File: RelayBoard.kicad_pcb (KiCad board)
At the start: 4 copper layers, 254 x 105.6 mm, 151 parts, among them J1 CONN_03-SCREW-5MM, J11 CONN_03-SCREW-5MM, J12 CONN_03-SCREW-5MM, J13 CONN_03-SCREW-5MM, J14 CONN_03-SCREW-5MM, J15 CONN_03-SCREW-5MM, J16 CONN_03-SCREW-5MM, J17 CONN_03-SCREW-5MM, J18 CONN_03-SCREW-5MM, J2 CONN_03-SCREW-5MM, J22 Conn_01x04, J24 Conn_01x06, J3 CONN_03-SCREW-5MM, J4 CONN_03-SCREW-5MM, J5 CONN_03-SCREW-5MM, J6 CONN_03-SCREW-5MM, J7 CONN_03-SCREW-5MM, J8 CONN_03-SCREW-5MM, K1 SANYOU_SRD_Form_C, K11 SANYOU_SRD_Form_C, K12 SANYOU_SRD_Form_C, K13 SANYOU_SRD_Form_C, K14 SANYOU_SRD_Form_C, K15 SANYOU_SRD_Form_C, K16 SANYOU_SRD_Form_C, K17 SANYOU_SRD_Form_C, K18 SANYOU_SRD_Form_C, K2 SANYOU_SRD_Form_C, K3 SANYOU_SRD_Form_C, K4 SANYOU_SRD_Form_C, K5 SANYOU_SRD_Form_C, K6 SANYOU_SRD_Form_C, K7 SANYOU_SRD_Form_C, K8 SANYOU_SRD_Form_C, Q1 ULN2803ADWR, Q2 ULN2803ADWR, U1 AP1117-33, U2 NodeMCUDevKitV1, U3 LTV-847, U4 LTV-847, U5 LTV-847, U6 LTV-847

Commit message: basic design with solid state relays complete
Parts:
- removed D11, D111, D112, D113, D114, D115, D116, D117, D118, D12, D13, D14, D15, D16, D17, D18: 1N4148W, Diode_SMD:D_SOD-123
- removed K1, K11, K12, K13, K14, K15, K16, K17, K18, K2, K3, K4, K5, K6, K7, K8: SANYOU_SRD_Form_C, Relay_THT:Relay_SPDT_SANYOU_SRD_Series_Form_C
- removed R1, R2: 22, Resistor_SMD:R_0402_1005Metric
- removed R12, R13, R14, R15, R16, R17, R18, R19, R20, R21, R22, R23, R24, R25, R26, R27: 150, Resistor_SMD:R_0402_1005Metric
- removed R3: 1.3k, Resistor_SMD:R_0402_1005Metric
- added U1: TLP148G, Package_SO:MFSOP6-5_4.4x3.6mm_P1.27mm, F.Cu at (140.0, 80.9)
- added U11: TLP148G, Package_SO:MFSOP6-5_4.4x3.6mm_P1.27mm, F.Cu at (157.5, 81.8)
- added U12: TLP148G, Package_SO:MFSOP6-5_4.4x3.6mm_P1.27mm, F.Cu at (174.9, 81.9)
- added U13: TLP148G, Package_SO:MFSOP6-5_4.4x3.6mm_P1.27mm, F.Cu at (192.1, 82.2)
- added U14: TLP148G, Package_SO:MFSOP6-5_4.4x3.6mm_P1.27mm, F.Cu at (209.8, 82.2)
- added U15: TLP148G, Package_SO:MFSOP6-5_4.4x3.6mm_P1.27mm, F.Cu at (210.0, 145.5)
- added U16: TLP148G, Package_SO:MFSOP6-5_4.4x3.6mm_P1.27mm, F.Cu at (192.5, 145.3)
- added U17: TLP148G, Package_SO:MFSOP6-5_4.4x3.6mm_P1.27mm, F.Cu at (175.2, 145.3)
- added U18: TLP148G, Package_SO:MFSOP6-5_4.4x3.6mm_P1.27mm, F.Cu at (157.5, 145.4)
- added U2: TLP148G, Package_SO:MFSOP6-5_4.4x3.6mm_P1.27mm, F.Cu at (122.4, 81.0)
- added U7: TLP148G, Package_SO:MFSOP6-5_4.4x3.6mm_P1.27mm, F.Cu at (105.0, 145.9)
- added U8: TLP148G, Package_SO:MFSOP6-5_4.4x3.6mm_P1.27mm, F.Cu at (87.5, 146.1)
- U3, U4, U5, U6: value LTV-847 -> TLP148G; footprint digikey-footprints:DIP-16_W7.62mm -> Package_SO:MFSOP6-5_4.4x3.6mm_P1.27mm
- moved J8 180.4 mm to (92.5, 155.4), turned to 180 degrees
- moved D38 178.8 mm to (87.5, 140.9), turned to -90 degrees
- moved R208 176.6 mm to (86.0, 140.9), turned to 90 degrees
- moved R108 164.9 mm to (89.1, 140.9), turned to 90 degrees
- moved J7 149.4 mm to (110.0, 155.3), turned to 180 degrees
- moved D37 142.0 mm to (105.0, 140.8), turned to -90 degrees
- moved R207 141.2 mm to (103.4, 140.8), turned to 90 degrees
- moved Q1 137.4 mm to (84.6, 117.4), turned to 180 degrees
- moved R4 129.5 mm to (28.2, 154.0), turned to 90 degrees
- moved R107 129.0 mm to (106.6, 140.8), turned to 90 degrees
- moved J14 124.0 mm to (204.8, 72.6), turned to 0 degrees
- moved J6 122.4 mm to (127.4, 155.0), turned to 180 degrees
- moved R214 116.7 mm to (211.3, 87.3), turned to -90 degrees
- moved D314 116.1 mm to (209.8, 87.3), turned to 90 degrees
- moved D36 108.6 mm to (122.4, 140.6), turned to -90 degrees
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- renumbered U2 to UM2, U1 to UP1
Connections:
- Q1 pad 11: Net-(Q1-Pad11) -> Net-(R108-Pad1)
- Q1 pad 12: Net-(Q1-Pad12) -> Net-(R107-Pad1)
- Q1 pad 13: Net-(Q1-Pad13) -> Net-(R106-Pad1)
- Q1 pad 14: Net-(Q1-Pad14) -> Net-(R105-Pad1)
- Q1 pad 15: Net-(Q1-Pad15) -> Net-(R103-Pad1)
- Q1 pad 16: Net-(Q1-Pad16) -> Net-(R104-Pad1)
- Q1 pad 17: Net-(Q1-Pad17) -> Net-(R102-Pad1)
- Q1 pad 18: Net-(Q1-Pad18) -> Net-(R101-Pad1)
- Q2 pad 11: Net-(Q2-Pad11) -> Net-(R118-Pad1)
- Q2 pad 13: Net-(Q2-Pad13) -> Net-(R116-Pad1)
- Q2 pad 14: Net-(Q2-Pad14) -> Net-(R115-Pad1)
- Q2 pad 15: Net-(Q2-Pad15) -> Net-(R114-Pad1)
- Q2 pad 16: Net-(Q2-Pad16) -> Net-(R113-Pad1)
- Q2 pad 17: Net-(Q2-Pad17) -> Net-(R112-Pad1)
- Q2 pad 18: Net-(Q2-Pad18) -> Net-(R111-Pad1)
- R101 pad 1: Net-(D11-Pad1) -> Net-(R101-Pad1)
- R102 pad 1: Net-(D12-Pad1) -> Net-(R102-Pad1)
- R103 pad 1: Net-(D13-Pad1) -> Net-(R103-Pad1)
- R104 pad 1: Net-(D14-Pad1) -> Net-(R104-Pad1)
- R105 pad 1: Net-(D15-Pad1) -> Net-(R105-Pad1)
- R106 pad 1: Net-(D16-Pad1) -> Net-(R106-Pad1)
- R107 pad 1: Net-(D17-Pad1) -> Net-(R107-Pad1)
- R108 pad 1: Net-(D18-Pad1) -> Net-(R108-Pad1)
- R111 pad 1: Net-(D111-Pad1) -> Net-(R111-Pad1)
- R112 pad 1: Net-(D112-Pad1) -> Net-(R112-Pad1)
- R113 pad 1: Net-(D113-Pad1) -> Net-(R113-Pad1)
- R114 pad 1: Net-(D114-Pad1) -> Net-(R114-Pad1)
- R115 pad 1: Net-(D115-Pad1) -> Net-(R115-Pad1)
- R116 pad 1: Net-(D116-Pad1) -> Net-(R116-Pad1)
- R117 pad 1: Net-(D117-Pad1) -> Net-(Q2-Pad12)
- R118 pad 1: Net-(D118-Pad1) -> Net-(R118-Pad1)
- U3 pad 1: Net-(Q1-Pad18) -> Net-(R103-Pad1)
- U3 pad 3: Net-(Q1-Pad17) -> Net-(D33-Pad2)
- U3 pad 4: Net-(R20-Pad2) -> Net-(J3-Pad3)
- U3 pad 5: Net-(Q1-Pad16) -> Net-(J3-Pad2)
- U3 pad 6: Net-(R21-Pad2) -> Net-(J3-Pad1)
- U4 pad 1: Net-(Q2-Pad18) -> Net-(R104-Pad1)
- U4 pad 3: Net-(Q2-Pad17) -> Net-(D34-Pad2)
- U4 pad 4: Net-(R13-Pad2) -> Net-(J4-Pad3)
- U4 pad 5: Net-(Q2-Pad16) -> Net-(J4-Pad2)
- U4 pad 6: Net-(R14-Pad2) -> Net-(J4-Pad1)
- U5 pad 1: Net-(Q1-Pad14) -> Net-(R105-Pad1)
- U5 pad 3: Net-(Q1-Pad13) -> Net-(D35-Pad2)
- U5 pad 4: Net-(R24-Pad2) -> Net-(J5-Pad3)
- U5 pad 5: Net-(Q1-Pad12) -> Net-(J5-Pad2)
- U5 pad 6: Net-(R25-Pad2) -> Net-(J5-Pad1)
- U6 pad 1: Net-(Q2-Pad14) -> Net-(R106-Pad1)
- U6 pad 3: Net-(Q2-Pad13) -> Net-(D36-Pad2)
- U6 pad 4: Net-(R17-Pad2) -> Net-(J6-Pad3)
- U6 pad 5: Net-(Q2-Pad12) -> Net-(J6-Pad2)
- U6 pad 6: Net-(R18-Pad2) -> Net-(J6-Pad1)
- UM2 pad 10: unconnected-(U2-Pad10) -> LED3
- UM2 pad 11: unconnected-(U2-Pad11) -> LED4
- UM2 pad 3: (no net) -> VBUS
- UM2 pad 4: (no net) -> MCU_VCC
- UM2 pad 5: unconnected-(U2-Pad5) -> LED1
- UM2 pad 6: (no net) -> GND
- UM2 pad 8: unconnected-(U2-Pad8) -> LED2
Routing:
- net Net-(Q1-Pad1): track 0.00 -> 107.7 mm
- net Net-(Q1-Pad2): track 0.00 -> 102.7 mm
- net Net-(Q2-Pad1): track 0.00 -> 97.9 mm, vias 0 -> 1
- net Net-(Q1-Pad3): track 0.00 -> 97.8 mm
- net Net-(Q2-Pad2): track 0.00 -> 96.7 mm, vias 0 -> 1
- net Net-(Q2-Pad3): track 0.00 -> 95.6 mm, vias 0 -> 1
- net Net-(Q2-Pad4): track 0.00 -> 94.3 mm, vias 0 -> 1
- net Net-(Q2-Pad5): track 0.00 -> 93.2 mm, vias 0 -> 1
- net Net-(Q1-Pad4): track 0.00 -> 92.7 mm
- net Net-(Q2-Pad6): track 0.00 -> 91.9 mm, vias 0 -> 1
- net Net-(Q2-Pad7): track 0.00 -> 90.8 mm, vias 0 -> 1
- net Net-(Q2-Pad8): track 0.00 -> 90.7 mm, vias 0 -> 1
- net Net-(Q1-Pad5): track 0.00 -> 87.8 mm
- net Net-(Q1-Pad6): track 0.00 -> 82.8 mm
- net Net-(R115-Pad1): track 0.00 -> 79.7 mm
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- added copper zone on F.Cu, net GND
- added copper zone on In1.Cu, net GND
- added copper zone on B.Cu, net MCU_VCC
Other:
- board size 254 x 105.6 mm -> 210.4 x 94.7 mm

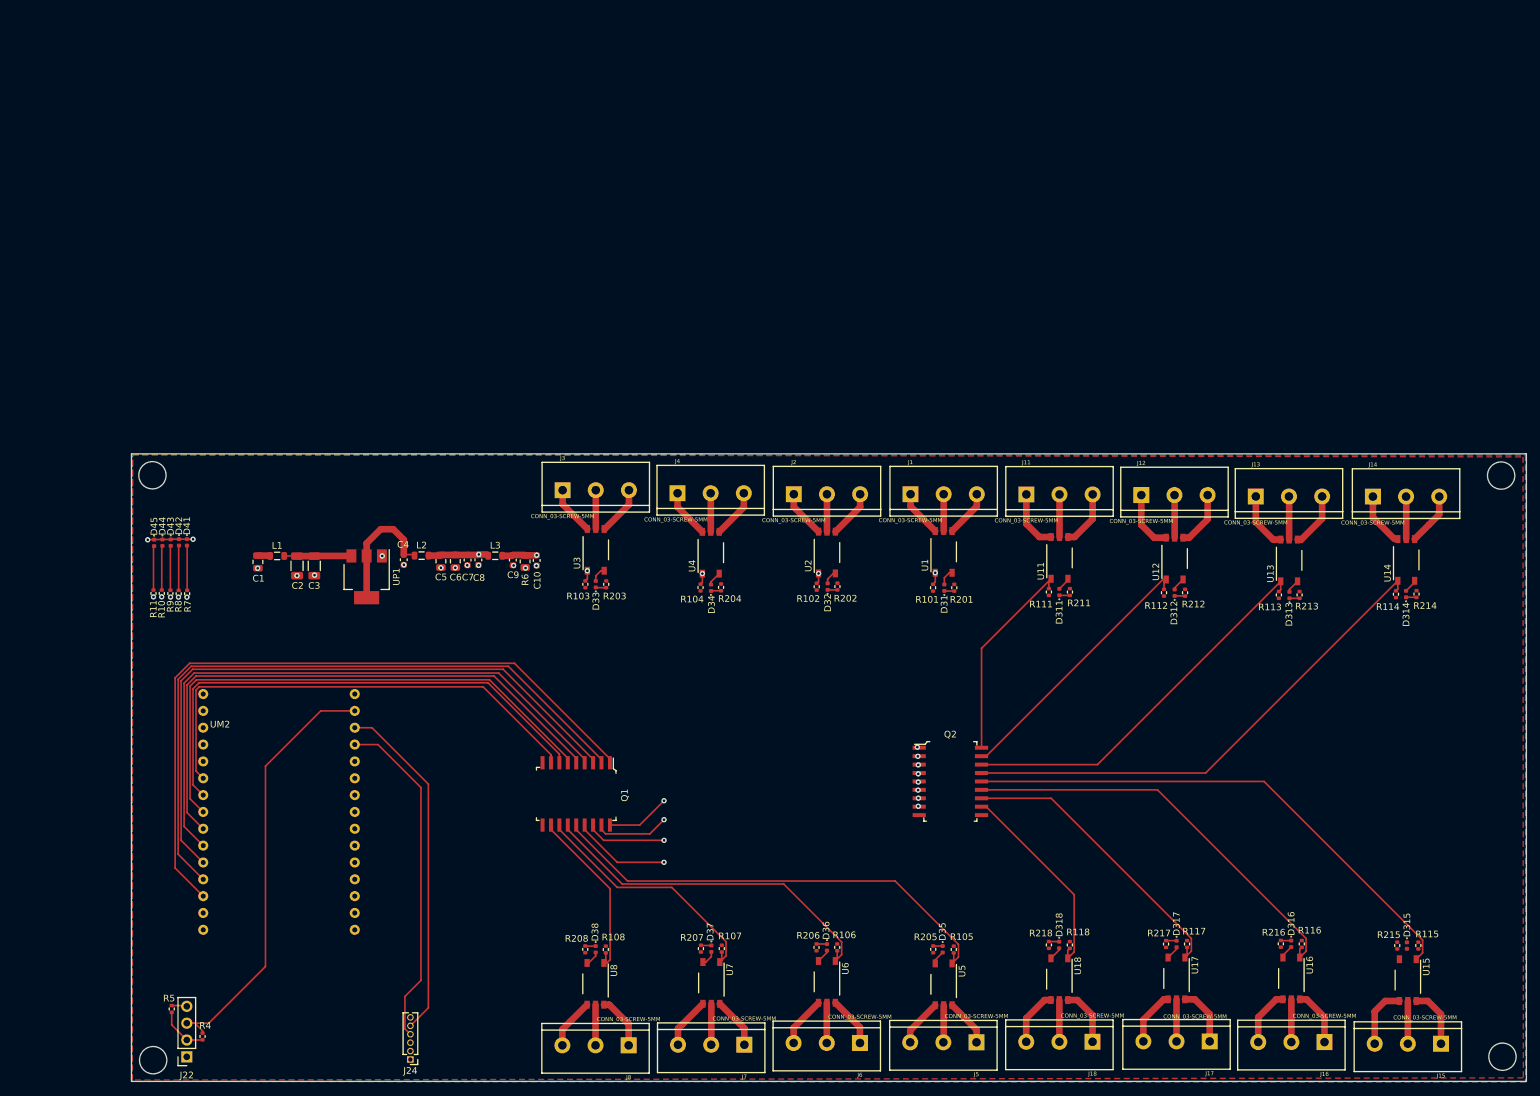
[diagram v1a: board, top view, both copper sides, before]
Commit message: remove esp32 and add Raspberry PI, along with AC power suppply
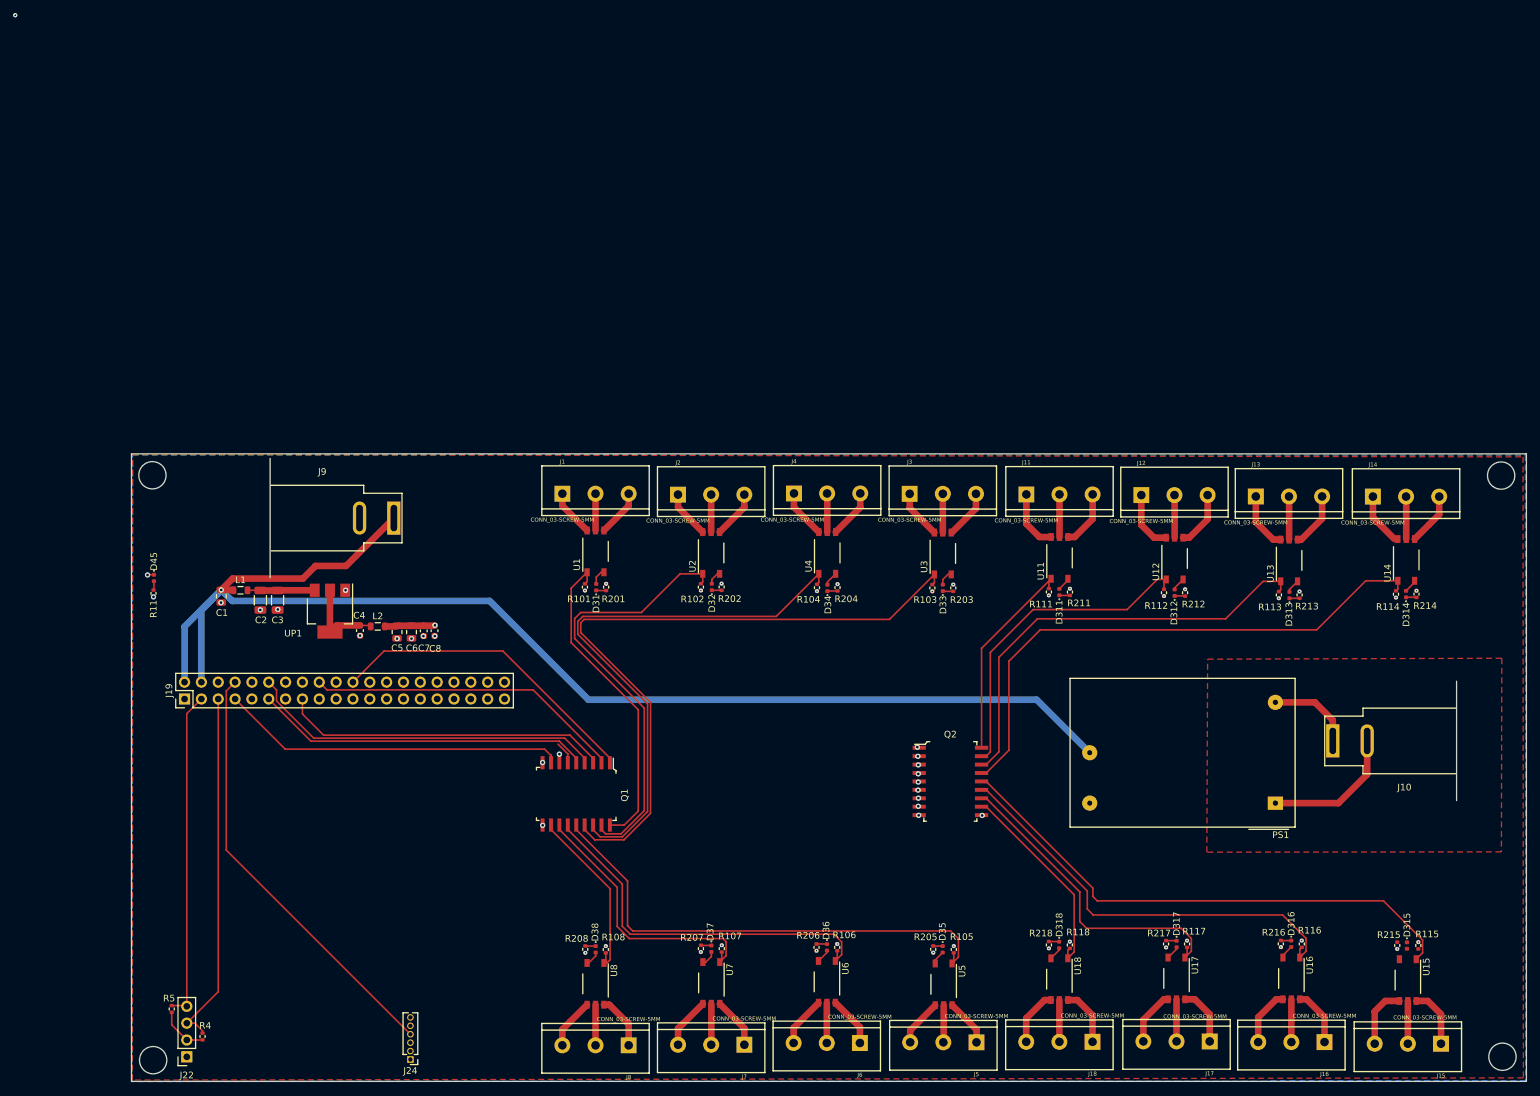
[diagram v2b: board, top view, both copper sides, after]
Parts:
- removed C10, C9: 1n, Capacitor_SMD:C_0603_1608Metric
- removed D41: LED1, LED_SMD:LED_0402_1005Metric
- removed D42: LED2, LED_SMD:LED_0402_1005Metric
- removed D43: LED3, LED_SMD:LED_0402_1005Metric
- removed D44: LED4, LED_SMD:LED_0402_1005Metric
- removed L3: 10uH, Inductor_SMD:L_0805_2012Metric
- removed R10, R7, R8, R9: 22, Resistor_SMD:R_0402_1005Metric
- removed R6: 1k, Resistor_SMD:R_0805_2012Metric
- removed UM2: NodeMCUDevKitV1, ESP32-footprints-Lib:NodeMCUDevKit1
- added J10: 24VAC Input, Connector_BarrelJack:BarrelJack_SwitchcraftConxall_RAPC10U_Horizontal, F.Cu at (198.7, 109.5)
- added J19: Raspberry_Pi_2_3, Connector_PinHeader_2.54mm:PinHeader_2x20_P2.54mm_Vertical, F.Cu at (25.5, 103.1)
- added J9: DC Input, Connector_BarrelJack:BarrelJack_SwitchcraftConxall_RAPC10U_Horizontal, F.Cu at (57.1, 75.8)
- added PS1: IRM-02-5, Converter_ACDC:Converter_ACDC_MeanWell_IRM-02-xx_THT, F.Cu at (190.1, 118.8)
- moved D31 52.5 mm to (87.6, 86.3)
- moved J1 52.5 mm to (82.5, 72.2)
- moved R201 52.5 mm to (89.1, 86.3)
- moved R101 52.5 mm to (85.9, 86.3)
- moved U1 52.5 mm to (87.5, 80.9)
- moved J3 52.3 mm to (134.9, 72.2)
- moved R203 52.3 mm to (141.5, 86.4)
- moved D33 52.3 mm to (139.9, 86.4)
- moved R103 52.3 mm to (138.3, 86.4)
- moved U3 52.3 mm to (139.9, 81.2)
- moved D34 17.6 mm to (122.5, 86.4)
- moved R104 17.6 mm to (120.9, 86.3)
- moved J4 17.6 mm to (117.5, 72.1)
- moved R204 17.6 mm to (124.0, 86.3)
- moved U4 17.6 mm to (122.5, 81.1)
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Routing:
- net VBUS: track 1.86 -> 204.9 mm, vias 0 -> 1
- net Net-(Q2-Pad1): track 97.9 -> 5.47 mm
- net Net-(Q2-Pad2): track 96.7 -> 5.62 mm
- net Net-(Q2-Pad3): track 95.6 -> 5.41 mm
- net Net-(Q2-Pad4): track 94.3 -> 5.36 mm
- net Net-(Q2-Pad5): track 93.2 -> 5.04 mm
- net Net-(Q2-Pad6): track 91.9 -> 4.80 mm
- net Net-(Q2-Pad8): track 90.7 -> 4.92 mm
- net Net-(Q2-Pad7): track 90.8 -> 5.04 mm
- net Net-(Q1-Pad6): track 82.8 -> 4.12 mm
- net Net-(Q1-Pad1): track 107.7 -> 48.1 mm
- net Net-(Q1-Pad2): track 102.7 -> 48.0 mm
- net Net-(Q1-Pad7): track 78.1 -> 28.3 mm, vias 0 -> 1
- net Net-(Q1-Pad3): track 97.8 -> 49.5 mm
- net Net-(Q1-Pad15): track 65.2 -> 104.0 mm, vias 2 -> 0
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- added copper zone on F.Cu, net (none)
